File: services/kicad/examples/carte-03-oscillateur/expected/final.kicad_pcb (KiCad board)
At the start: 2 copper layers, 50 x 35 mm, 15 parts, among them J1 PWR, J2 OUT, U1 NE555

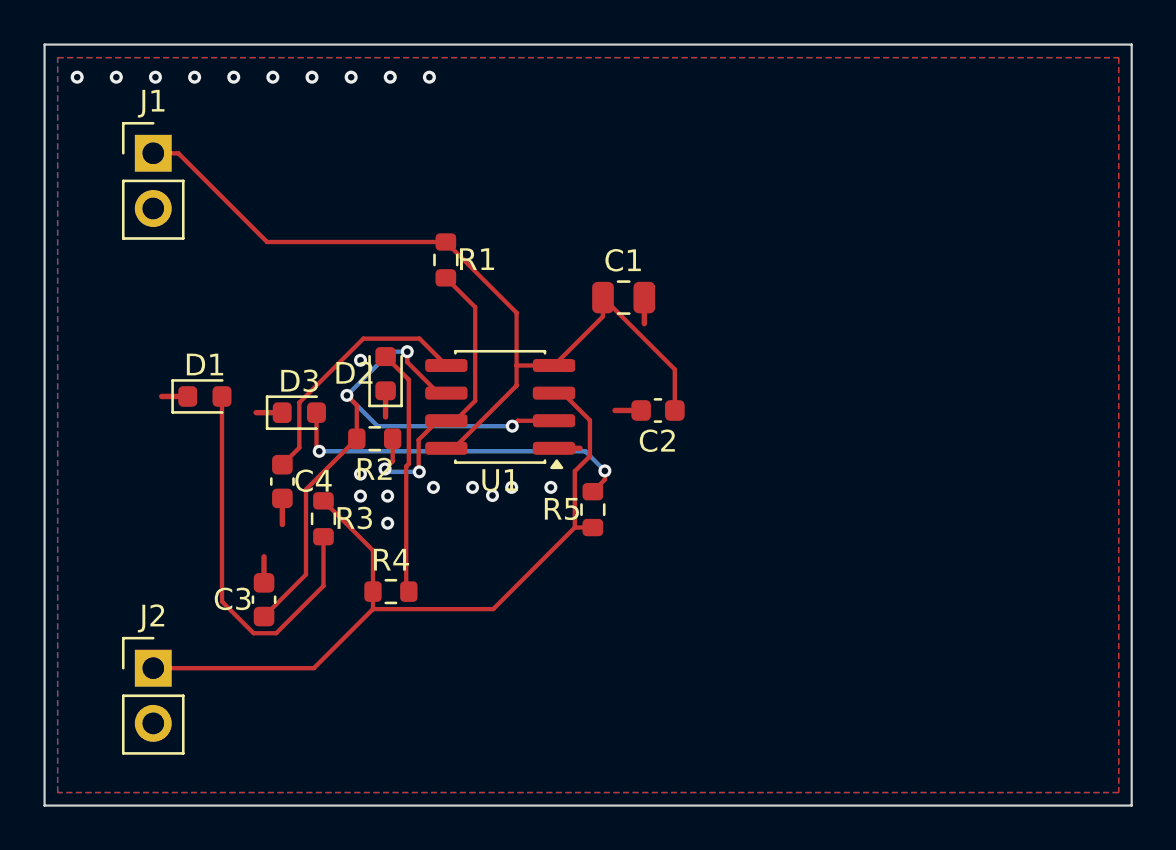
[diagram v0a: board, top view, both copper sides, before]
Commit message: test(examples): banc regenere -- placements livres, journaux et mesures a jour
- expected/placement.kicad_pcb ajoutes (carte-05, carte-06) et
  vue-dessus.png (carte-04) : le banc compare desormais le placement,
  pas seulement le board final.
- generer_exemples.py, regenerer_le_banc.py, livrer_placements.py,
  apercu_routage.py : regeneration reproductible du banc et rendus
  d apercu.
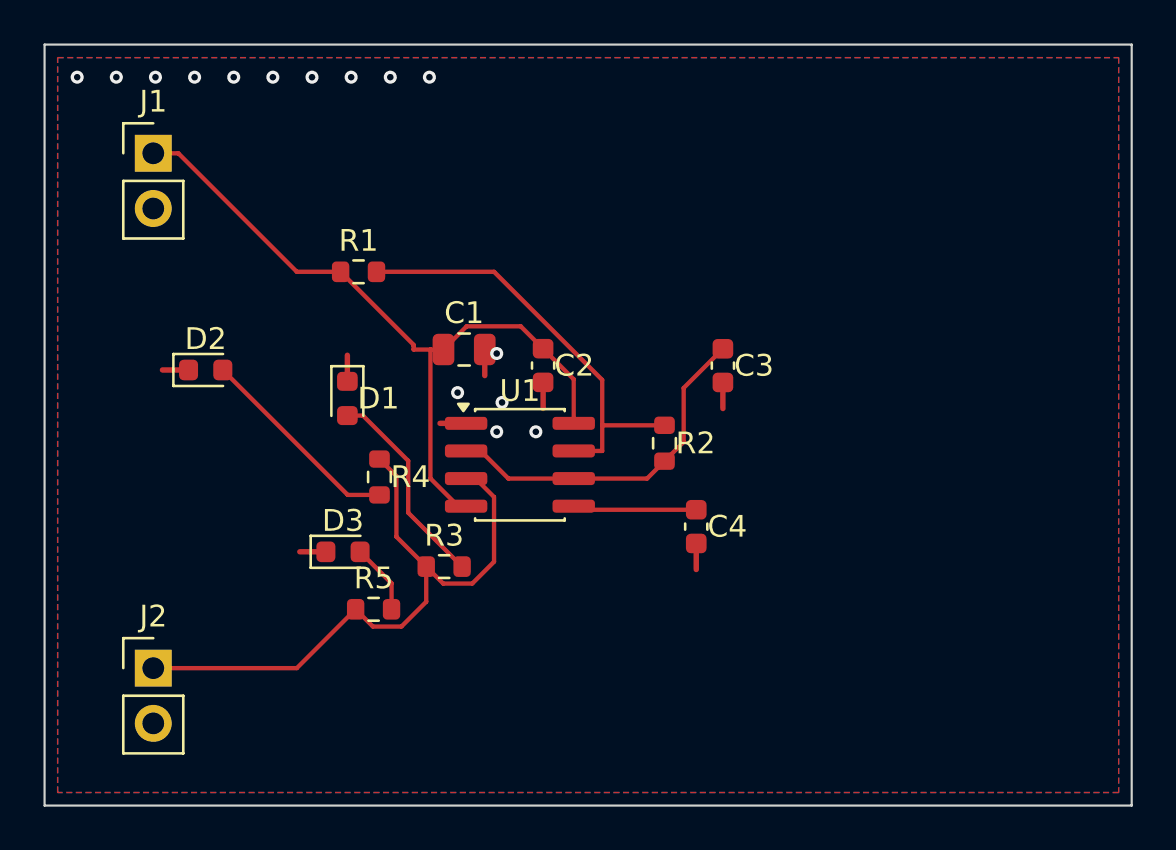
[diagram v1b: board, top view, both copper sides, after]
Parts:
- moved C3 23.7 mm to (154.7, 102.3), turned to -90 degrees
- moved C4 19.1 mm to (153.5, 109.7)
- moved R2 13.3 mm to (152.0, 105.8), turned to -90 degrees
- moved R5 11.1 mm to (138.6, 113.5), turned to 0 degrees
- moved D2 8.28 mm to (130.9, 102.5), turned to 0 degrees
- moved C1 7.72 mm to (142.8, 101.5)
- moved D3 6.71 mm to (137.2, 110.8)
- moved D1 6.55 mm to (137.4, 103.8), turned to -90 degrees
- moved R3 5.97 mm to (141.9, 111.5), turned to 0 degrees
- moved C2 5.67 mm to (146.4, 102.3), turned to -90 degrees
- moved R4 5.30 mm to (138.9, 107.4), turned to -90 degrees
- moved R1 4.05 mm to (137.9, 98.0), turned to 0 degrees
- moved U1 2.81 mm to (145.4, 106.8), turned to 0 degrees
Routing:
- net LED3_A: track 16.5 -> 3.24 mm, vias 2 -> 0
- net THRES: track 28.8 -> 16.3 mm, vias 3 -> 0
- net LED1_A: track 17.9 -> 9.55 mm
- net CTRL: track 11.7 -> 5.70 mm
- net OUT: track 36.2 -> 30.4 mm
- net DISCH: track 14.2 -> 19.9 mm, vias 2 -> 0
- net VCC: track 39.9 -> 34.8 mm
- net LED2_A: track 11.4 -> 9.59 mm
- net GND: vias 20 -> 15
